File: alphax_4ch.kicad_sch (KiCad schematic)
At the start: 235 parts, among them J1 USB_B_Mini, J2 Cortex_Debug, J3 Conn_01x01, J4 Conn_01x01, J5 Conn_01x01, J6 Conn_01x01, M1 Module-power12-0.2, M2 Module-power5-0.2, M3 Module-vr-discrete-0.1, M4 Module-ign8-0.1, M5 Module-input-0.1, M6 Module-mcu144-0.6, M7 Module-can-0.1, M8 Module-vr-discrete-0.1, P1 33311-24AW-2, P2 33311-24AW-2, Q1 AO3400A, Q10 AO3400A, Q11 AO3400A, Q12 AO3400A, Q13 AO3401A, Q14 AO3401A, Q15 AO3400A, Q16 AO3401A, Q17 AO3401A, Q18 AO3401A, Q19 AO3400A, Q2 AO3400A, Q20 AO3400A, Q21 AO3400A, Q22 VND14NV04-E, Q23 VND14NV04-E, Q24 AO3400A, Q25 AO3400A, Q26 VND14NV04-E, Q27 AO3400A, Q28 VND14NV04-E, Q29 VND14NV04-E, Q3 AO3401A, Q30 VND14NV04-E, Q31 AO3401A, Q32 AO3401A, Q33 AO3400A, Q34 AO3400A, Q35 AO3400A, Q36 AO3400A, Q4 AO3401A, Q5 AO3401A, Q6 VND14NV04-E, Q7 VND14NV04-E, Q8 VND14NV04-E, Q9 VND14NV04-E, U1 TLS115, U2 74HC2G17GW, U3 MPXH6400A, U4 JDY-33, U5 74HC2G17GW, U6 TLE9201SG

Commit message: tiny update
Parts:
- added J7, J8: Conn_01x01, MountingHole:MountingHole_4.5mm_Pad, symbol Connector_Generic:Conn_01x01
- R40: footprint hellen-one-common:SMD1206 -> hellen-one-common:R1206
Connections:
- net IN_FLEX: now also M5.S21 (IN_AUX4); no longer M5.S20 (IN_AUX3)
- no-connect marks 74 -> 76
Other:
- note added: "EINT1"
- note added: "EINT11"
- note added: "EINT12"
- note added: "EINT13"
- note added: "EINT14"
- note added: "EINT15"
- note added: "EINT2"
- note added: "EINT3"
- note added: "EINT4"
- note added: "EINT5"
- note added: "EINT6"
- note added: "EINT7"
- note added: "EINT9"

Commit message: update schem
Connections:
- net +12V: now also R5.1; no longer R5.4
- net FLEX: now also M5.N7 (AUX4), M6.S27 (IN_AUX4); no longer M5.N8 (AUX3), M6.S26 (IN_AUX3)
- net GND: now also R5.4; no longer R5.1
- net INJ3: now also R84.5; no longer R27.3
- net INJ4: now also R84.6; no longer R27.4
- net TPS1: no longer M5.N5 (PPS), M6.S29 (IN_PPS)
- net at D17.1 (A), D21.1 (K): now also R5.7; no longer R5.5
- net at D39.1 (A), D45.1 (K): now also R5.8; no longer R5.7
- net at D20.2 (K), D22.2 (A): now also R5.5; no longer R5.8
- new net: M5.N8 (AUX3), M6.S26 (IN_AUX3)
- new net PPS1: M5.N5 (PPS), M6.S29 (IN_PPS)
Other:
- moved on the sheet: D17, D21, D39, D40, D45, D46

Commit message: update
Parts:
- R49: value 4.7k -> 1k; LCSC C1980 -> C240722
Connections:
- net A2_2 is gone; now on net D2: P2.2 (D2), R70.2
- net A3_2 is gone; now on net D3: P2.3 (D3), R69.2
- net A4_2 is gone; now on net D4: P2.4 (D4), R68.2
- net A5_2 is gone; now on net D5: P2.5 (D5), R67.2
- net +5V: no longer R49.1, R49.2, R49.3, R49.4
- net CAM_VR_PULLUP: now also R49.3
- net CRANK_N_PULLUP: now also R49.2
- net CRANK_P_PULLUP: now also R49.1
- net D2: no longer M5.N26 (SENS1), M6.S8 (IN_SENS1)
- net D3: no longer M5.N25 (SENS2), M6.S9 (IN_SENS2)
- net D4: no longer M5.N24 (SENS3), M6.S10 (IN_SENS3)
- net D5: no longer M5.N23 (SENS4), M6.S11 (IN_SENS4)
- net A1_2 renamed D1
- net A6_2 renamed D6
- net A7_2 renamed D7
- net B1_2 renamed E1
- net B2_2 renamed E2
- net B3_2 renamed E3
- net B4_2 renamed E4
- net B5_2 renamed E5
- net B6_2 renamed E6
- net B7_2 renamed E7
- net B8_2 renamed E8
- net C1_2 renamed F1
- net C2_2 renamed F2
- net C3_2 renamed F3
- net C4_2 renamed F4
- net C5_2 renamed F5
- net C6_2 renamed F6
- net C7_2 renamed F7
- net C8_2 renamed F8
- new net DIG2: M5.N26 (SENS1), M6.S8 (IN_SENS1)
- new net DIG3: M5.N25 (SENS2), M6.S9 (IN_SENS2)
- new net DIG4: M5.N24 (SENS3), M6.S10 (IN_SENS3)
- new net DIG5: M5.N23 (SENS4), M6.S11 (IN_SENS4)
- no-connect marks 76 -> 77
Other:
- moved on the sheet: R49

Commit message: rev.A schematics & pcb files
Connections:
- net GND: now also Q20.3 (S), Q21.3 (S), Q33.3 (S), Q34.3 (S), Q35.3 (S), Q36.3 (S); no longer Q20.2 (D), Q21.2 (D), Q33.2 (D), Q34.2 (D), Q35.2 (D), Q36.2 (D)
- net at R82.1, R89.2: now also Q36.2 (D); no longer Q36.3 (S)
- net at R81.1, R88.2: now also Q35.2 (D); no longer Q35.3 (S)
- net at R42.1, R45.2: now also Q21.2 (D); no longer Q21.3 (S)
- net at R80.1, R87.2: now also Q34.2 (D); no longer Q34.3 (S)
- net at R29.1, R44.2: now also Q20.2 (D); no longer Q20.3 (S)
- net at R79.1, R86.2: now also Q33.2 (D); no longer Q33.3 (S)
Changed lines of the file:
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@@
   (title_block
     (title "AlphaECU 4chan powered by rusEFI")
-    (date "2022-03-13")
+    (date "2022-03-14")
     (rev "A")
     (company "rusEFI")
@@
     (pin "1")
   )
-  (symbol (lib_id "hellen-one-common:MOSFET-N") (at 346.71 358.14 0) (mirror x) (unit 1)
+  (symbol (lib_id "hellen-one-common:MOSFET-N") (at 346.71 358.14 0) (unit 1)
     (in_bom yes) (on_board yes)
-    (property "Reference" "Q36" (id 0) (at 351.79 356.87 0)
+    (property "Reference" "Q36" (id 0) (at 351.79 354.33 0)
       (effects (font (size 1.27 1.27)) (justify left))
     )
-    (property "Value" "AO3400A" (id 1) (at 351.79 359.41 0)
+    (property "Value" "AO3400A" (id 1) (at 351.79 356.87 0)
       (effects (font (size 1.27 1.27)) (justify left))
     )
-    (property "Footprint" "hellen-one-common:SOT-23" (id 2) (at 353.06 356.235 0)
+    (property "Footprint" "hellen-one-common:SOT-23" (id 2) (at 353.06 360.045 0)
       (effects (font (size 1.27 1.27) italic) (justify left) hide)
     )
@@
     (pin "2")
   )
-  (symbol (lib_id "hellen-one-common:MOSFET-N") (at 341.63 364.49 0) (mirror x) (unit 1)
+  (symbol (lib_id "hellen-one-common:MOSFET-N") (at 341.63 364.49 0) (unit 1)
     (in_bom yes) (on_board yes)
     (property "Reference" "Q35" (id 0) (at 330.2 360.68 0)
@@
       (effects (font (size 1.27 1.27)) (justify left))
     )
-    (property "Footprint" "hellen-one-common:SOT-23" (id 2) (at 347.98 362.585 0)
+    (property "Footprint" "hellen-one-common:SOT-23" (id 2) (at 347.98 366.395 0)
       (effects (font (size 1.27 1.27) italic) (justify left) hide)
     )
@@
     (pin "1")
   )
-  (symbol (lib_id "hellen-one-common:MOSFET-N") (at 267.97 297.18 0) (mirror x) (unit 1)
+  (symbol (lib_id "hellen-one-common:MOSFET-N") (at 267.97 297.18 0) (unit 1)
     (in_bom yes) (on_board yes)
     (property "Reference" "Q21" (id 0) (at 273.05 295.91 0)
@@
       (effects (font (size 1.27 1.27)) (justify left))
     )
-    (property "Footprint" "hellen-one-common:SOT-23" (id 2) (at 274.32 295.275 0)
+    (property "Footprint" "hellen-one-common:SOT-23" (id 2) (at 274.32 299.085 0)
       (effects (font (size 1.27 1.27) italic) (justify left) hide)
     )
@@
     (pin "2")
   )
-  (symbol (lib_id "hellen-one-common:MOSFET-N") (at 336.55 372.11 0) (mirror x) (unit 1)
+  (symbol (lib_id "hellen-one-common:MOSFET-N") (at 336.55 372.11 0) (unit 1)
     (in_bom yes) (on_board yes)
     (property "Reference" "Q34" (id 0) (at 330.2 367.03 0)
@@
       (effects (font (size 1.27 1.27)) (justify left))
     )
-    (property "Footprint" "hellen-one-common:SOT-23" (id 2) (at 342.9 370.205 0)
+    (property "Footprint" "hellen-one-common:SOT-23" (id 2) (at 342.9 374.015 0)
       (effects (font (size 1.27 1.27) italic) (justify left) hide)
     )
@@
     (pin "1")
   )
-  (symbol (lib_id "hellen-one-common:MOSFET-N") (at 331.47 378.46 0) (mirror x) (unit 1)
+  (symbol (lib_id "hellen-one-common:MOSFET-N") (at 331.47 378.46 0) (unit 1)
     (in_bom yes) (on_board yes)
-    (property "Reference" "Q33" (id 0) (at 325.12 373.38 0)
+    (property "Reference" "Q33" (id 0) (at 326.39 373.38 0)
       (effects (font (size 1.27 1.27)) (justify left))
     )
-    (property "Value" "AO3400A" (id 1) (at 321.31 375.92 0)
+    (property "Value" "AO3400A" (id 1) (at 322.58 375.92 0)
       (effects (font (size 1.27 1.27)) (justify left))
     )
-    (property "Footprint" "hellen-one-common:SOT-23" (id 2) (at 337.82 376.555 0)
+    (property "Footprint" "hellen-one-common:SOT-23" (id 2) (at 337.82 380.365 0)
       (effects (font (size 1.27 1.27) italic) (justify left) hide)
     )
@@
     (pin "2")
   )
-  (symbol (lib_id "hellen-one-common:MOSFET-N") (at 262.89 303.53 0) (mirror x) (unit 1)
+  (symbol (lib_id "hellen-one-common:MOSFET-N") (at 262.89 303.53 0) (unit 1)
     (in_bom yes) (on_board yes)
     (property "Reference" "Q20" (id 0) (at 271.78 302.26 0)
       (effects (font (size 1.27 1.27)) (justify left))
     )
-    (property "Value" "AO3400A" (id 1) (at 271.78 304.8 0)
+    (property "Value" "AO3400A" (id 1) (at 271.9642 304.3982 0)
       (effects (font (size 1.27 1.27)) (justify left))
     )
-    (property "Footprint" "hellen-one-common:SOT-23" (id 2) (at 269.24 301.625 0)
+    (property "Footprint" "hellen-one-common:SOT-23" (id 2) (at 269.24 305.435 0)
       (effects (font (size 1.27 1.27) italic) (justify left) hide)
     )

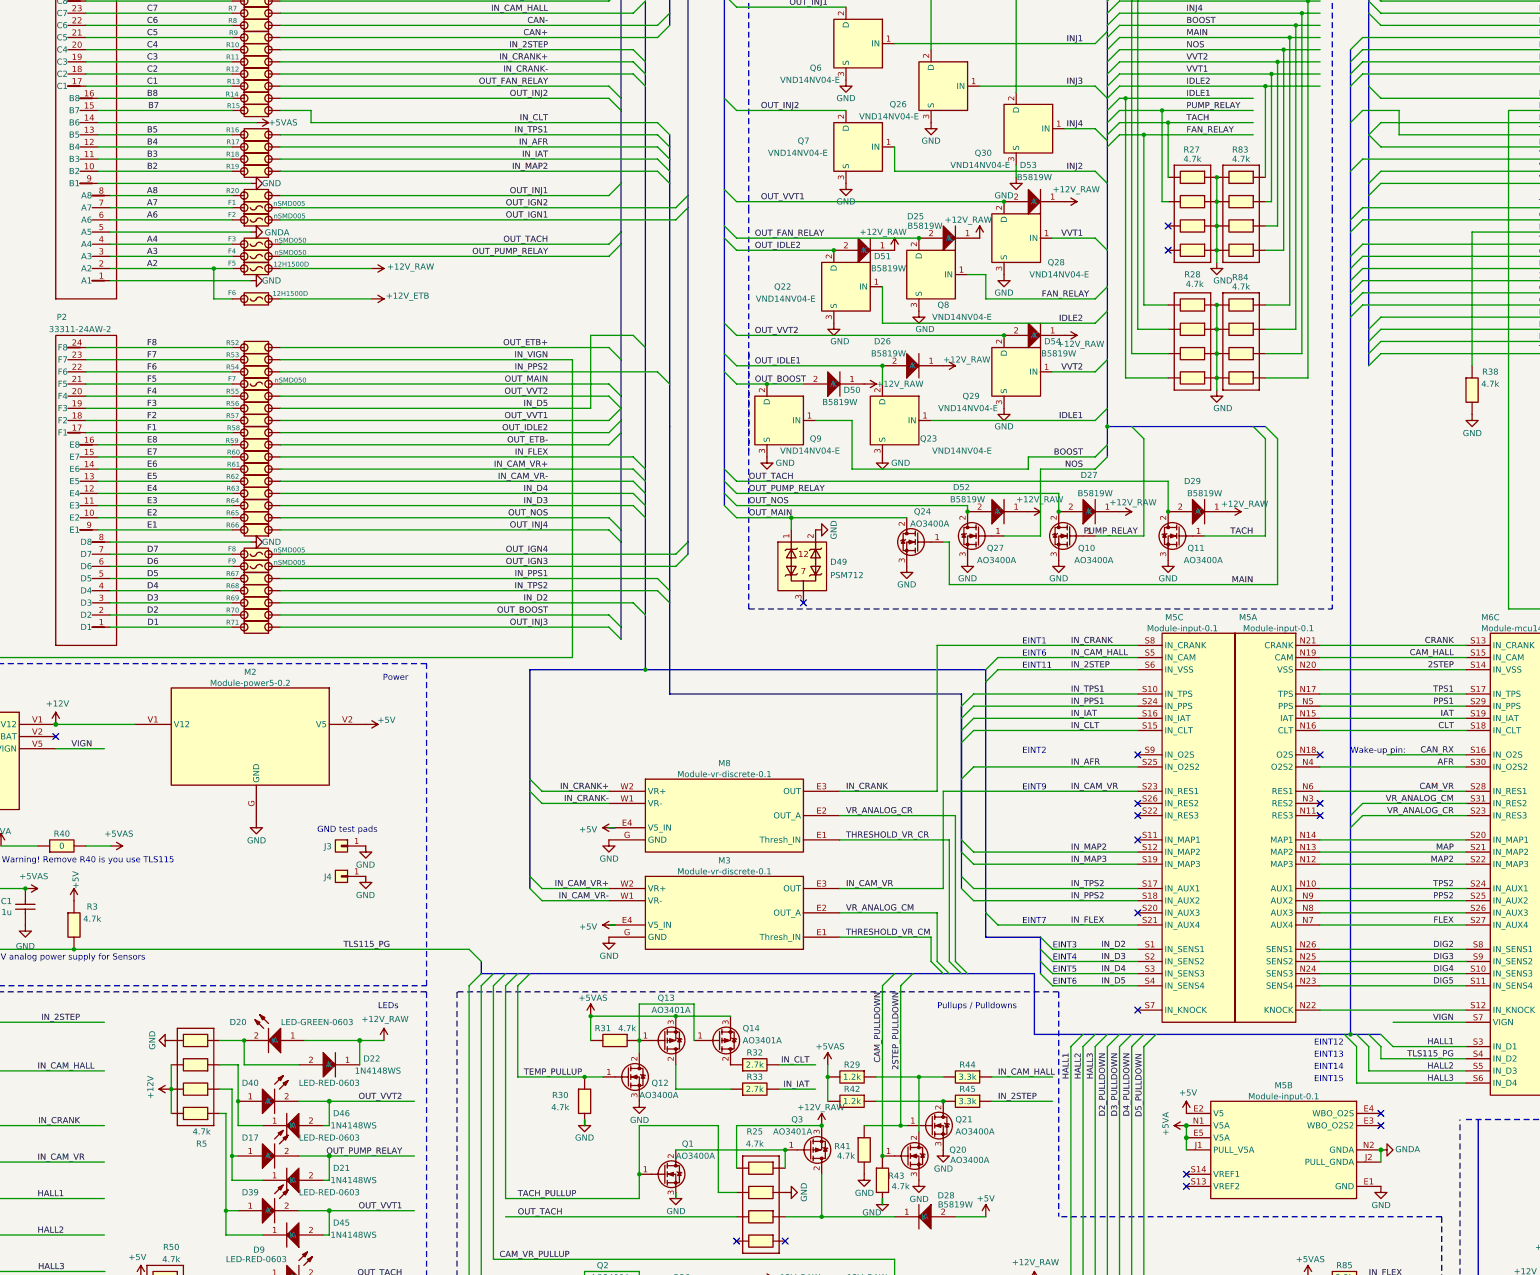
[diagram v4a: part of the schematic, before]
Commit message: https://github.com/rusefi/alphax-4chan/issues/10 https://github.com/rusefi/alphax-4chan/issues/9 https://github.com/rusefi/alphax-4chan/issues/12
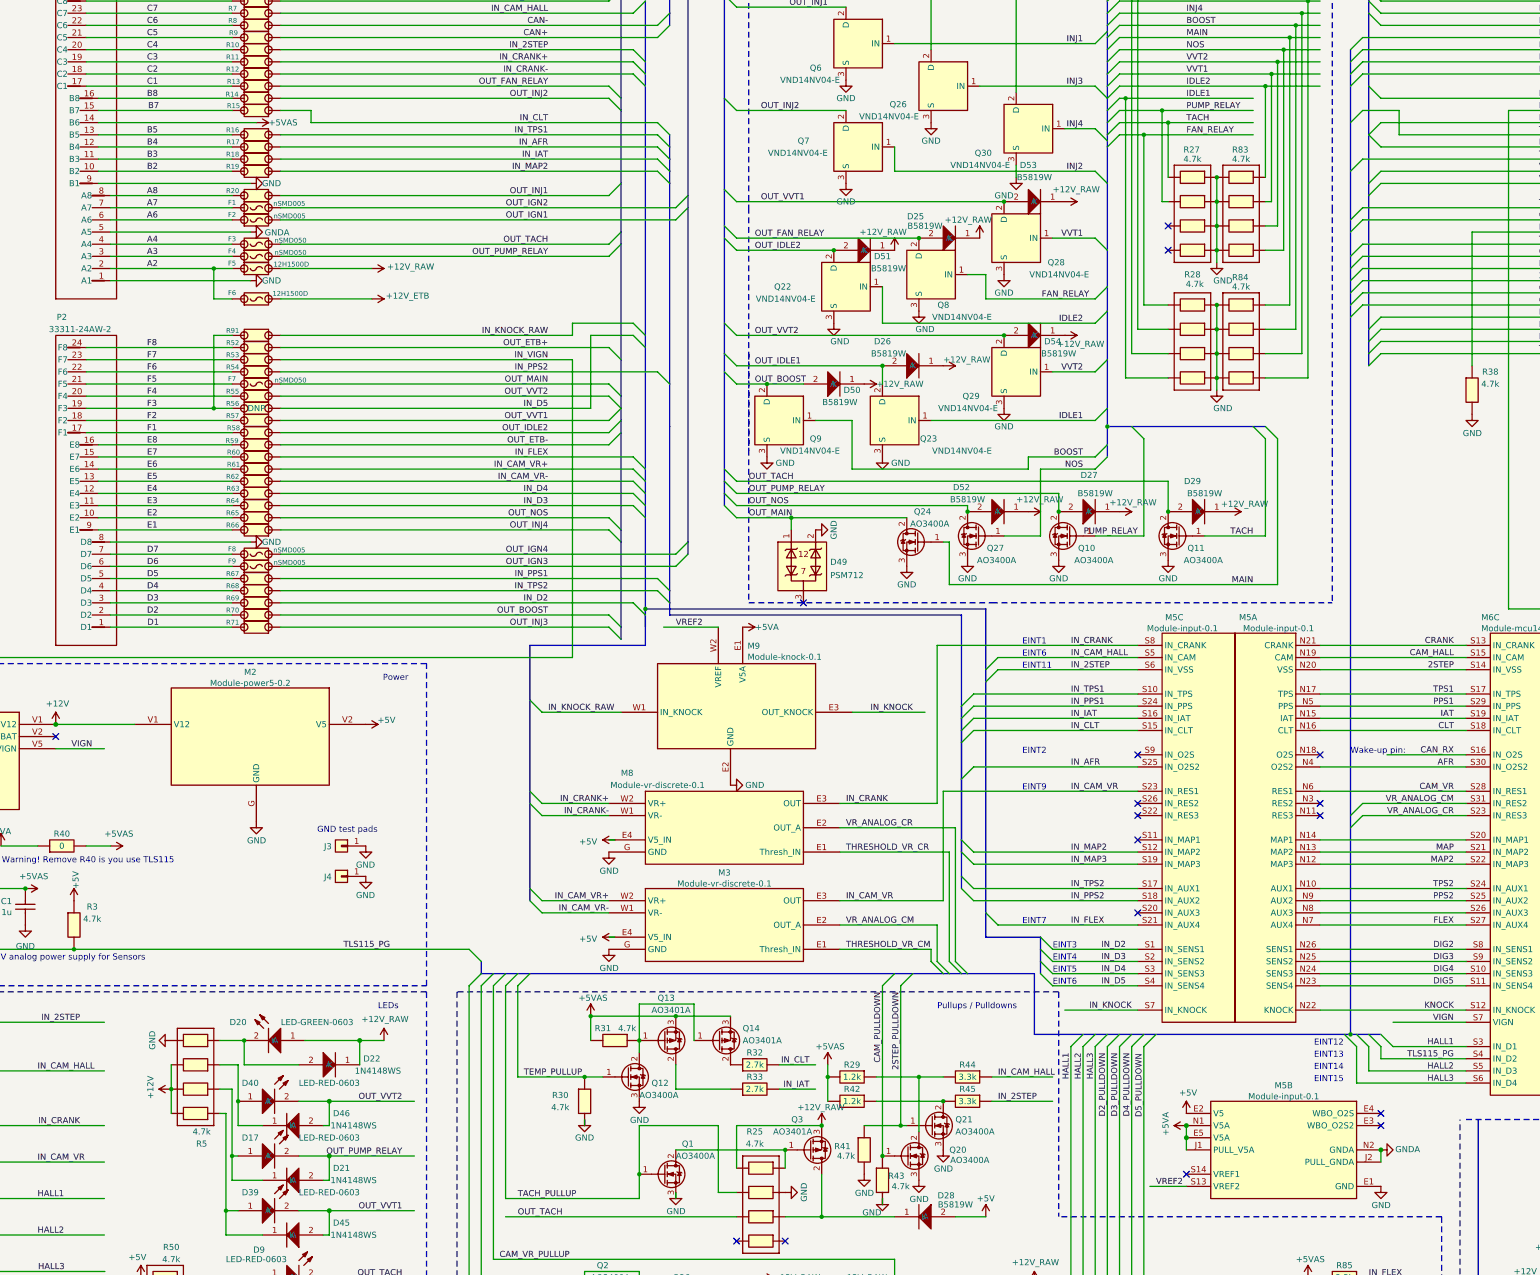
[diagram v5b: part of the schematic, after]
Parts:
- added M9: Module-knock-0.1, hellen-one-knock-0.1:knock, symbol hellen-one-knock-0.1:Module-knock-0.1
- added R91: Jumper-Pad-Pad, hellen-one-common:PAD-0805-PAD, symbol hellen-one-common:Jumper-Pad-Pad
- R56: LCSC C17477 -> (none); MyComment (none) -> DNP
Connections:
- net +5VA: now also M9.E1 (V5A)
- net F3: now also R91.2
- net GND: now also M9.E2 (GND)
- net KNOCK: now reaches M5.N22 (KNOCK), M6.S12 (IN_KNOCK)
- net IN_KNOCK: now reaches M5.S7 (IN_KNOCK)
- net IN_KNOCK: now also M9.E3 (OUT_KNOCK)
- net VREF2: now reaches M5.S13 (VREF2)
- net VREF2: now also M9.W2 (VREF)
- new net IN_KNOCK_RAW: M9.W1 (IN_KNOCK), R91.1
- no-connect marks 77 -> 75
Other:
- moved on the sheet: M3, M8

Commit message: update rev.B
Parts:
- removed R47, R48: 0, hellen-one-common:R0603, symbol hellen-one-common:Res
- added U7: SN74LVC1G06DBVR, Package_TO_SOT_SMD:SOT-23-5, symbol 74xGxx:74LVC1G06
- D49: value PSM712 -> PSM712-LF
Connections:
- net +3V3: now also U7.5 (V)
- net +5V: now also R46.2; no longer R46.1
- net CAN_RX: now also U7.2; no longer M6.S16 (IN_O2S)
- net CAN_TX: no longer R46.2
- net GND: now also U7.3 (GND)
- net CAN_VIO: now reaches M6.N1 (CAN_VIO)
- net CAN_VIO: now also M7.V2 (CAN_VIO)
- new net WAKEUP: M6.S16 (IN_O2S), R46.1, U7.4

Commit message: rev.C release candidate
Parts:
- added C17: 100n, hellen-one-common:C0603, symbol hellen-one-common:Cap
- added D55: PSM712-LF, hellen-one-common:SOT-23, symbol hellen-one-common:PSM712
- added D56: B5819W, hellen-one-common:SOD-123, symbol hellen-one-common:1N4148WS
- added R47: 2k, hellen-one-common:R1206, symbol hellen-one-common:Res
- added R48, R92, R93: 4.7k, hellen-one-common:R0603, symbol hellen-one-common:Res
- M4: value Module-ign8-0.1 -> Module-ign8-0.2; footprint hellen-one-ign8-0.1:ign8 -> hellen-one-ign8-0.2:ign8
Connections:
- net +12V_RAW: now also R47.2; no longer Q16.2 (D), Q3.3 (S), Q31.2 (D), Q4.2 (D), R25.1
- net GND: now also R25.6, C17.1, D55.3; no longer R25.7
- net OUT_TACH: now also R25.4; no longer R25.3
- net TACH_PULLUP: now also R25.3; no longer R25.2
- net at Q31.1 (G), Q32.1 (G), R76.1: now also R93.2; no longer Q25.2 (D)
- net at Q3.1 (G), R25.8: now also R25.7; no longer Q1.2 (D)
- net at Q16.1 (G), Q17.1 (G), R26.4: now also R48.2; no longer Q15.2 (D)
- net at Q4.1 (G), Q5.1 (G), R26.1: now also R92.2; no longer Q2.2 (D)
- net at R25.5: now also D28.1 (K), D56.1 (K)
- new net: D56.2 (A), Q3.2 (D)
- new net: Q25.2 (D), R93.1
- new net: Q15.2 (D), R48.1
- new net: Q1.2 (D), R25.2
- new net: Q2.2 (D), R92.1
- new net +12V_LIM: C17.2, D55.1, Q16.2 (D), Q3.3 (S), Q31.2 (D), Q4.2 (D), R25.1, R47.1
- no-connect marks 75 -> 74
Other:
- moved on the sheet: Q15, Q2, Q25, Q3, R25, R74
